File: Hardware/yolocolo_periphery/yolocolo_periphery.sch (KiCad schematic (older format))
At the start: 6 parts

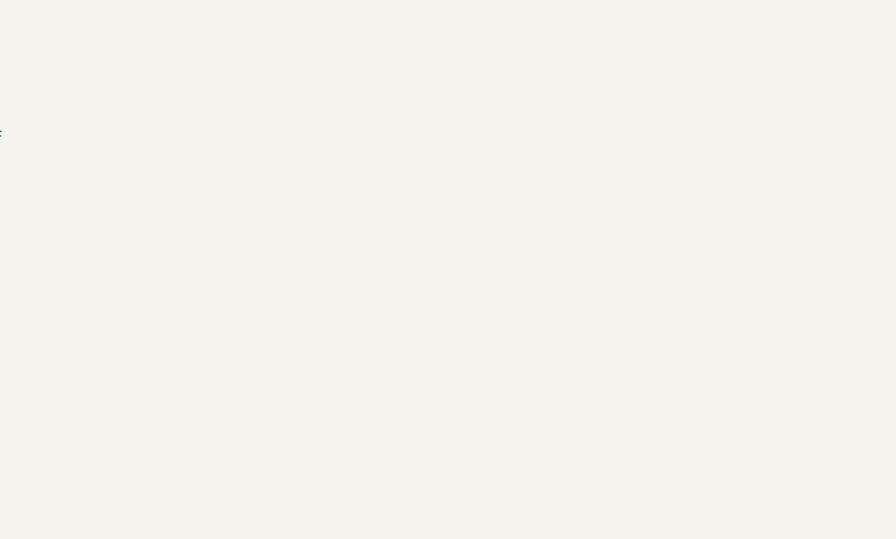
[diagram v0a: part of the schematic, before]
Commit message: Plugged in Shift-Register
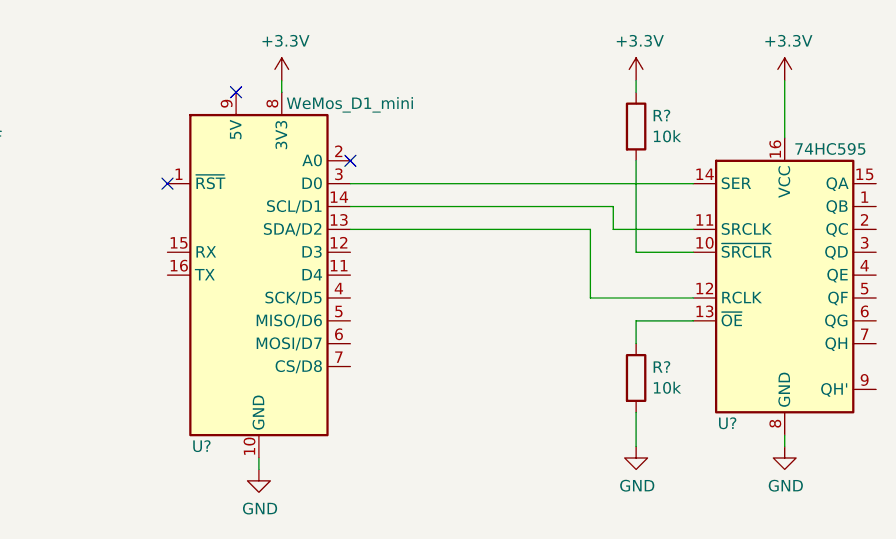
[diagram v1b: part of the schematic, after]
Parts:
- added R? (x2): 10k, symbol Device:R
- added U?: WeMos_D1_mini, Module:WEMOS_D1_mini_light, symbol MCU_Module:WeMos_D1_mini
- added U?: 74HC595, symbol 74xx:74HC595
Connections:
- net +3V3: now also R?.1, U?.16 (VCC), U?.8 (3V3)
- net GND: now also R?.2, U?.10 (GND), U?.8 (GND)
- new net: U?.12 (RCLK), U?.13 (SDA/D2)
- new net: U?.11 (SRCLK), U?.14 (SCL/D1)
- new net: U?.14 (SER), U?.3 (D0)
- new net: R?.2, U?.10 (~SRCLR)
- new net: R?.1, U?.13 (~OE)
- no-connect marks 0 -> 3
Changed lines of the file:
@@
 Wire Wire Line
 	3250 1400 3250 1500
+$Comp
+L MCU_Module:WeMos_D1_mini U?
+U 1 1 5D318183
+P 5750 1850
+F 0 "U?" H 5500 1100 50  0000 C CNN
+F 1 "WeMos_D1_mini" H 6150 2600 50  0000 C CNN
+F 2 "Module:WEMOS_D1_mini_light" H 5750 700 50  0001 C CNN
+F 3 "https://wiki.wemos.cc/products:d1:d1_mini#documentation" H 3900 700 50  0001 C CNN
+	1    5750 1850
+	1    0    0    -1
+$EndComp
+NoConn ~ 5650 1050
+NoConn ~ 5350 1450
+$Comp
+L power:+3.3V #PWR?
+U 1 1 5D31ABB3
+P 5850 1000
+F 0 "#PWR?" H 5850 850 50  0001 C CNN
+F 1 "+3.3V" H 5865 1173 50  0000 C CNN
+F 2 "" H 5850 1000 50  0001 C CNN
+F 3 "" H 5850 1000 50  0001 C CNN
+	1    5850 1000
+	1    0    0    -1
+$EndComp
+Wire Wire Line
+	5850 1000 5850 1050
+$Comp
+L power:GND #PWR?
+U 1 1 5D31B6D3
+P 5750 2700
+F 0 "#PWR?" H 5750 2450 50  0001 C CNN
+F 1 "GND" H 5755 2527 50  0000 C CNN
+F 2 "" H 5750 2700 50  0001 C CNN
+F 3 "" H 5750 2700 50  0001 C CNN
+	1    5750 2700
+	1    0    0    -1
+$EndComp
+Wire Wire Line
+	5750 2700 5750 2650
+NoConn ~ 6150 1350
+$Comp
+L 74xx:74HC595 U?
+U 1 1 5D31E54A
+P 8050 1850
+F 0 "U?" H 7800 1200 50  0000 C CNN
+F 1 "74HC595" H 8250 2400 50  0000 C CNN
+F 2 "" H 8050 1850 50  0001 C CNN
+F 3 "http://www.ti.com/lit/ds/symlink/sn74hc595.pdf" H 8050 1850 50  0001 C CNN
+	1    8050 1850
+	1    0    0    -1
+$EndComp
+$Comp
+L power:+3.3V #PWR?
+U 1 1 5D31F4E4
+P 8050 1000
+F 0 "#PWR?" H 8050 850 50  0001 C CNN
+F 1 "+3.3V" H 8065 1173 50  0000 C CNN
+F 2 "" H 8050 1000 50  0001 C CNN
+F 3 "" H 8050 1000 50  0001 C CNN
+	1    8050 1000
+	1    0    0    -1
+$EndComp
+Wire Wire Line
+	8050 1000 8050 1250
+$Comp
+L power:GND #PWR?
+U 1 1 5D320AE6
+P 8050 2600
+F 0 "#PWR?" H 8050 2350 50  0001 C CNN
+F 1 "GND" H 8055 2427 50  0000 C CNN
+F 2 "" H 8050 2600 50  0001 C CNN
+F 3 "" H 8050 2600 50  0001 C CNN
+	1    8050 2600
+	1    0    0    -1
+$EndComp
+Wire Wire Line
+	8050 2600 8050 2550
+$Comp
+L Device:R R?
+U 1 1 5D323BC4
+P 7400 2300
+F 0 "R?" H 7470 2346 50  0000 L CNN
+F 1 "10k" H 7470 2255 50  0000 L CNN
+F 2 "" V 7330 2300 50  0001 C CNN
+F 3 "~" H 7400 2300 50  0001 C CNN
+	1    7400 2300
+	1    0    0    -1
+$EndComp
+Wire Wire Line
+	7400 2150 7400 2050
+Wire Wire Line
+	7400 2050 7650 2050
+$Comp
+L power:GND #PWR?
+U 1 1 5D32587A
+P 7400 2600
+F 0 "#PWR?" H 7400 2350 50  0001 C CNN
+F 1 "GND" H 7405 2427 50  0000 C CNN
+F 2 "" H 7400 2600 50  0001 C CNN
+F 3 "" H 7400 2600 50  0001 C CNN
+	1    7400 2600
+	1    0    0    -1
+$EndComp
+Wire Wire Line
+	7400 2600 7400 2450
+$Comp
+L Device:R R?
+U 1 1 5D327010
+P 7400 1200
+F 0 "R?" H 7470 1246 50  0000 L CNN
+F 1 "10k" H 7470 1155 50  0000 L CNN
+F 2 "" V 7330 1200 50  0001 C CNN
+F 3 "~" H 7400 1200 50  0001 C CNN
+	1    7400 1200
+	1    0    0    -1
+$EndComp
+$Comp
+L power:+3.3V #PWR?
+U 1 1 5D329F9F
+P 7400 1000
+F 0 "#PWR?" H 7400 850 50  0001 C CNN
+F 1 "+3.3V" H 7415 1173 50  0000 C CNN
+F 2 "" H 7400 1000 50  0001 C CNN
+F 3 "" H 7400 1000 50  0001 C CNN
+	1    7400 1000
+	1    0    0    -1
+$EndComp
+Wire Wire Line
+	7400 1050 7400 1000
+Wire Wire Line
+	7650 1750 7400 1750
+Wire Wire Line
+	7400 1750 7400 1350
+Wire Wire Line
+	6150 1450 7650 1450
+Wire Wire Line
+	6150 1550 7300 1550
+Wire Wire Line
+	7300 1550 7300 1650
+Wire Wire Line
+	7300 1650 7650 1650
+Wire Wire Line
+	6150 1650 7200 1650
+Wire Wire Line
+	7200 1650 7200 1950
+Wire Wire Line
+	7200 1950 7650 1950
 $EndSCHEMATC

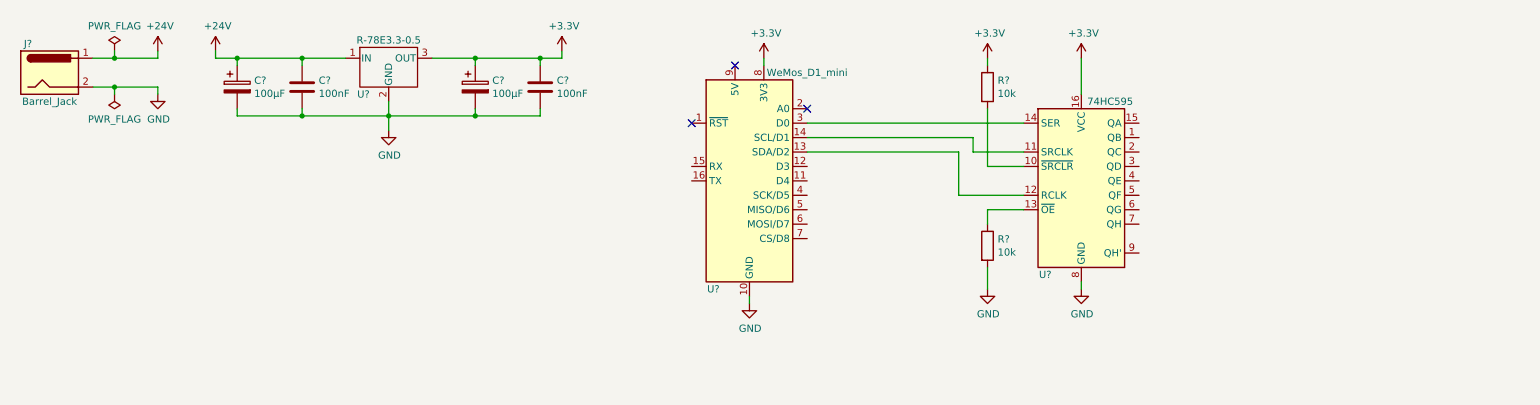
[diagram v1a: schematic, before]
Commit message: Routed RJ45-Connector
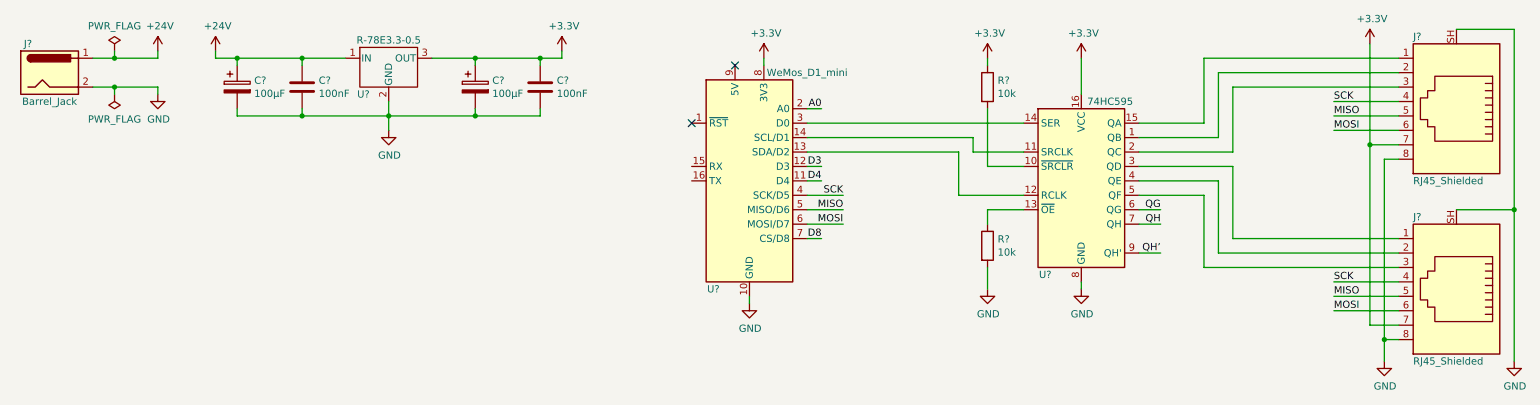
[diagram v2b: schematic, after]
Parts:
- added J? (x2): RJ45_Shielded, symbol Connector:RJ45_Shielded
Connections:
- net +3V3: now also J?.7, J?.7
- net GND: now also J?.8, J?.8, J?.SH, J?.SH
- net D4: now reaches U?.11 (D4)
- net D3: now reaches U?.12 (D3)
- net A0: now reaches U?.2 (A0)
- net SCK: now reaches U?.4 (SCK/D5)
- net SCK: now also J?.4, J?.4
- net MISO: now reaches U?.5 (MISO/D6)
- net MISO: now also J?.5, J?.5
- net MOSI: now reaches U?.6 (MOSI/D7)
- net MOSI: now also J?.6, J?.6
- net D8: now reaches U?.7 (CS/D8)
- net at U?.1 (QB): now also J?.2
- net at U?.15 (QA): now also J?.1
- net at U?.2 (QC): now also J?.3
- net at U?.3 (QD): now also J?.1
- net at U?.4 (QE): now also J?.2
- net at U?.5 (QF): now also J?.3
- net QG: now reaches U?.6 (QG)
- net QH: now reaches U?.7 (QH)
- net QH’: now reaches U?.9 (QH')
- no-connect marks 3 -> 2
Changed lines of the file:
@@
 Wire Wire Line
 	5750 2700 5750 2650
-NoConn ~ 6150 1350
 $Comp
 L 74xx:74HC595 U?
@@
 Wire Wire Line
 	7200 1950 7650 1950
+Text Label 6250 1350 2    50   ~ 0
+A0
+Text Label 6250 1750 2    50   ~ 0
+D3
+Text Label 6250 1850 2    50   ~ 0
+D4
+Text Label 6250 2250 2    50   ~ 0
+D8
+Wire Wire Line
+	6250 2250 6150 2250
+Wire Wire Line
+	6250 1850 6150 1850
+Wire Wire Line
+	6250 1750 6150 1750
+Wire Wire Line
+	6150 1350 6250 1350
+Text Label 6400 1950 2    50   ~ 0
+SCK
+Text Label 6400 2050 2    50   ~ 0
+MISO
+Text Label 6400 2150 2    50   ~ 0
+MOSI
+Wire Wire Line
+	6400 1950 6150 1950
+Wire Wire Line
+	6150 2050 6400 2050
+Wire Wire Line
+	6400 2150 6150 2150
+$Comp
+L Connector:RJ45_Shielded J?
+U 1 1 5D31A5A1
+P 10650 2550
+F 0 "J?" H 10950 2100 50  0000 R CNN
+F 1 "RJ45_Shielded" H 10950 3100 50  0000 R CNN
+F 2 "" V 10650 2575 50  0001 C CNN
+F 3 "~" V 10650 2575 50  0001 C CNN
+	1    10650 2550
+	-1   0    0    1
+$EndComp
+$Comp
+L Connector:RJ45_Shielded J?
+U 1 1 5D31BE76
+P 10650 1300
+F 0 "J?" H 10950 850 50  0000 R CNN
+F 1 "RJ45_Shielded" H 10950 1850 50  0000 R CNN
+F 2 "" V 10650 1325 50  0001 C CNN
+F 3 "~" V 10650 1325 50  0001 C CNN
+	1    10650 1300
+	-1   0    0    1
+$EndComp
+$Comp
+L power:GND #PWR?
+U 1 1 5D328061
+P 11050 3100
+F 0 "#PWR?" H 11050 2850 50  0001 C CNN
+F 1 "GND" H 11055 2927 50  0000 C CNN
+F 2 "" H 11050 3100 50  0001 C CNN
+F 3 "" H 11050 3100 50  0001 C CNN
+	1    11050 3100
+	1    0    0    -1
+$EndComp
+Wire Wire Line
+	11050 3100 11050 2050
+Wire Wire Line
+	11050 2050 10650 2050
+Wire Wire Line
+	11050 2050 11050 800
+Wire Wire Line
+	11050 800  10650 800
+Connection ~ 11050 2050
+$Comp
+L power:GND #PWR?
+U 1 1 5D3311E3
+P 10150 3100
+F 0 "#PWR?" H 10150 2850 50  0001 C CNN
+F 1 "GND" H 10155 2927 50  0000 C CNN
+F 2 "" H 10150 3100 50  0001 C CNN
+F 3 "" H 10150 3100 50  0001 C CNN
+	1    10150 3100
+	1    0    0    -1
+$EndComp
+Wire Wire Line
+	10150 3100 10150 2950
+Wire Wire Line
+	10150 2950 10250 2950
+Wire Wire Line
+	10150 1700 10250 1700
+Connection ~ 10150 2950
+$Comp
+L power:+3.3V #PWR?
+U 1 1 5D33366C
+P 10050 900
+F 0 "#PWR?" H 10050 750 50  0001 C CNN
+F 1 "+3.3V" H 10065 1073 50  0000 C CNN
+F 2 "" H 10050 900 50  0001 C CNN
+F 3 "" H 10050 900 50  0001 C CNN
+	1    10050 900
+	1    0    0    -1
+$EndComp
+Wire Wire Line
+	10250 1600 10050 1600
+Wire Wire Line
+	10050 1600 10050 900
+Wire Wire Line
+	10050 2850 10050 1600
+Connection ~ 10050 1600
+Wire Wire Line
+	10250 2850 10050 2850
+Wire Wire Line
+	10150 2950 10150 1700
+Text Label 9800 2550 0    50   ~ 0
+SCK
+Text Label 9800 2650 0    50   ~ 0
+MISO
+Text Label 9800 2750 0    50   ~ 0
+MOSI
+Wire Wire Line
+	9800 2550 10250 2550
+Wire Wire Line
+	10250 2650 9800 2650
+Wire Wire Line
+	9800 2750 10250 2750
+Text Label 9800 1300 0    50   ~ 0
+SCK
+Text Label 9800 1400 0    50   ~ 0
+MISO
+Text Label 9800 1500 0    50   ~ 0
+MOSI
+Wire Wire Line
+	9800 1300 10250 1300
+Wire Wire Line
+	10250 1400 9800 1400
+Wire Wire Line
+	9800 1500 10250 1500
+Wire Wire Line
+	8450 1450 8900 1450
+Wire Wire Line
+	8900 1450 8900 1000
+Wire Wire Line
+	8900 1000 10250 1000
+Wire Wire Line
+	9000 1550 9000 1100
+Wire Wire Line
+	9000 1100 10250 1100
+Wire Wire Line
+	8450 1550 9000 1550
+Wire Wire Line
+	8450 1650 9100 1650
+Wire Wire Line
+	9100 1650 9100 1200
+Wire Wire Line
+	9100 1200 10250 1200
+Wire Wire Line
+	9100 2250 10250 2250
+Wire Wire Line
+	9000 2350 10250 2350
+Wire Wire Line
+	9000 1850 8450 1850
+Wire Wire Line
+	9000 1850 9000 2350
+Wire Wire Line
+	9100 1750 8450 1750
+Wire Wire Line
+	9100 1750 9100 2250
+Wire Wire Line
+	10250 2450 8900 2450
+Wire Wire Line
+	8900 2450 8900 1950
+Wire Wire Line
+	8900 1950 8450 1950
+Text Label 8600 2050 2    50   ~ 0
+QG
+Wire Wire Line
+	8600 2050 8450 2050
+Text Label 8600 2150 2    50   ~ 0
+QH
+Wire Wire Line
+	8600 2150 8450 2150
+Text Label 8600 2350 2    50   ~ 0
+QH’
+Wire Wire Line
+	8600 2350 8450 2350
 $EndSCHEMATC
